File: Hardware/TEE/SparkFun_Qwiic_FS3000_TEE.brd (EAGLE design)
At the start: 25.4 x 25.4 mm, 53 parts, among them J2 QWIIC_RA, U1 FS3000

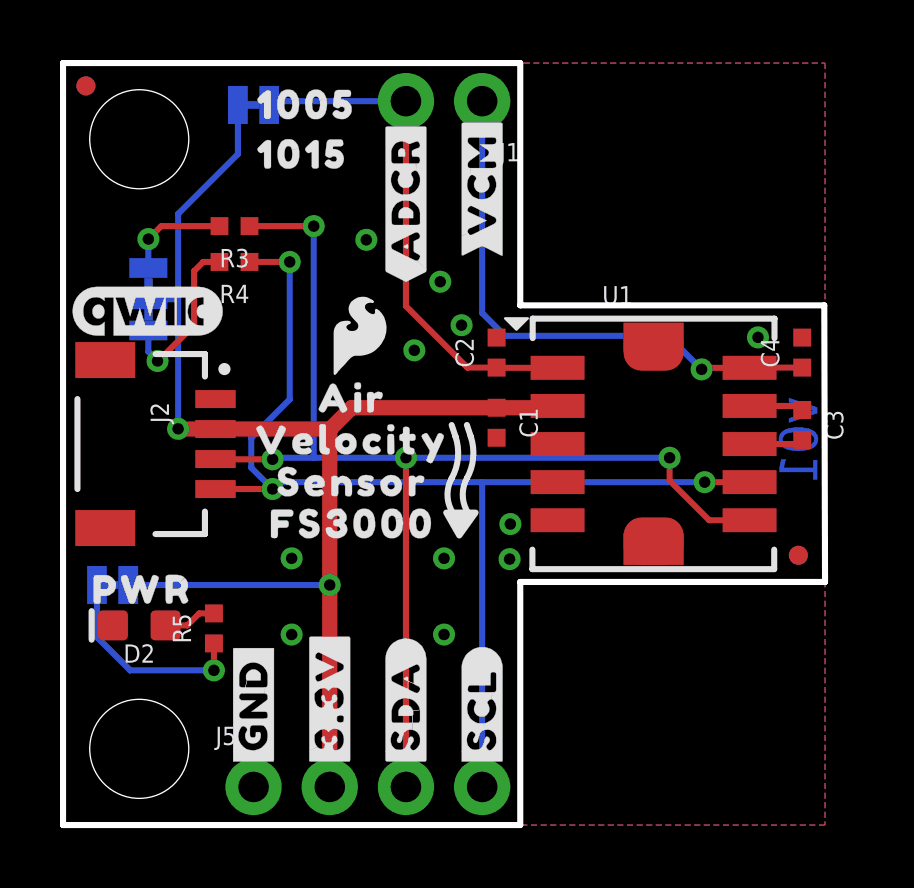
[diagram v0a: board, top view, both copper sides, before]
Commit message: eng ran checklist before double-check request
-dimensions were off grid slightly, corrected [1X1 version].
-approved DRC overlap error on jumper [1X1 version].
-added a couple more stitching GND vias [1X1]
-updated pad 3 to extend longer as shown in datasheet [both versions]
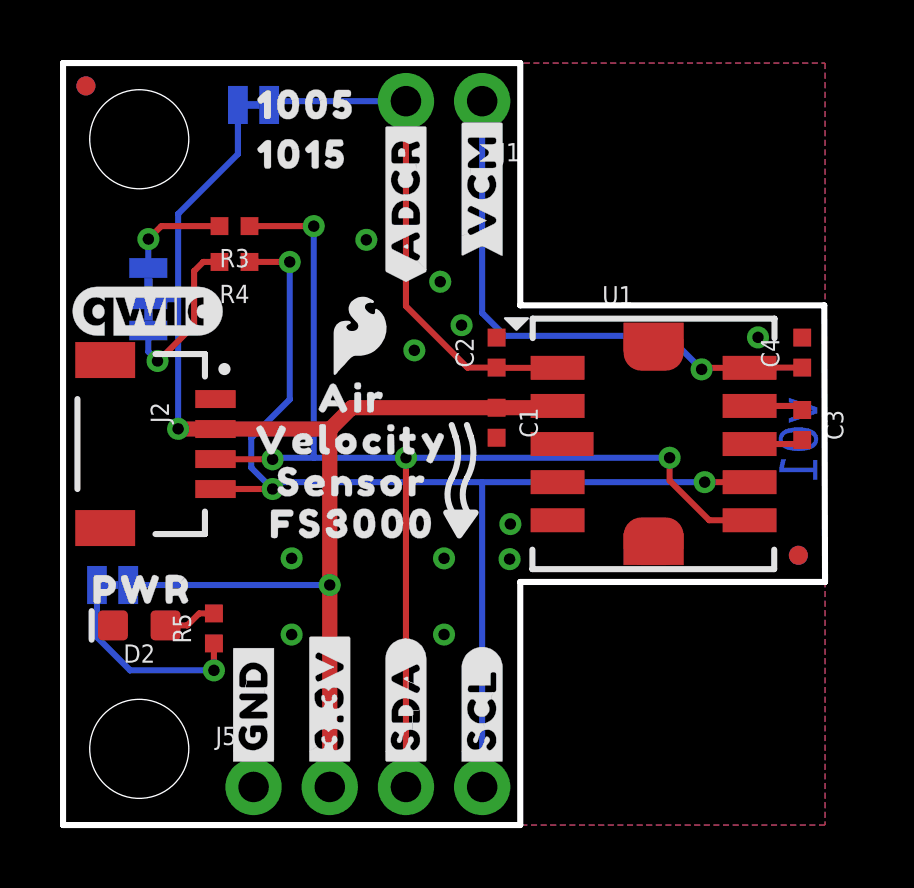
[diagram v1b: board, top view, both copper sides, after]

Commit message: updated some stuff to correct recent libraries
-GNDs, Fiducials, and standoffs were still in old library. updated.
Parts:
- JP11, JP2, JP5, JP6: device SparkFun:MICRO-FIDUCIAL -> SparkFun-Aesthetics:FIDUCIAL-MICRO
- JP3, JP8: device SparkFun:STAND-OFF -> SparkFun-Hardware:STAND-OFF
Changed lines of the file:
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@@
 <drawing>
 <settings>
-<setting alwaysvectorfont="yes"/>
+<setting alwaysvectorfont="no"/>
 <setting keepoldvectorfont="yes"/>
 <setting verticaltext="up"/>
@@
 <layer number="47" name="Measures" color="7" fill="1" visible="no" active="yes"/>
 <layer number="48" name="Document" color="7" fill="1" visible="no" active="yes"/>
-<layer number="49" name="Reference" color="7" fill="1" visible="yes" active="yes"/>
+<layer number="49" name="Reference" color="7" fill="1" visible="no" active="yes"/>
 <layer number="50" name="dxf" color="7" fill="1" visible="no" active="yes"/>
 <layer number="51" name="tDocu" color="6" fill="1" visible="yes" active="yes"/>
@@
 </autorouter>
 <elements>
-<element name="JP3" library="SparkFun" package="STAND-OFF" value="STAND-OFF" x="2.54" y="22.86" smashed="yes"/>
-<element name="JP2" library="SparkFun" package="MICRO-FIDUCIAL" value="FIDUCIALUFIDUCIAL" x="24.511" y="8.9916" smashed="yes"/>
-<element name="JP6" library="SparkFun" package="MICRO-FIDUCIAL" value="FIDUCIALUFIDUCIAL" x="0.762" y="24.638" smashed="yes"/>
+<element name="JP3" library="SparkFun-Hardware" package="STAND-OFF" value="STAND-OFF" x="2.54" y="22.86" smashed="yes"/>
+<element name="JP2" library="SparkFun-Aesthetics" package="FIDUCIAL-MICRO" value="FIDUCIALUFIDUCIAL" x="24.511" y="8.9916" smashed="yes"/>
+<element name="JP6" library="SparkFun-Aesthetics" package="FIDUCIAL-MICRO" value="FIDUCIALUFIDUCIAL" x="0.762" y="24.638" smashed="yes"/>
 <element name="R4" library="SparkFun-Resistors" package="0402-TIGHT" value="2.2k" x="5.715" y="18.7706" smashed="yes" rot="R180">
 <attribute name="NAME" x="5.715" y="18.0086" size="0.6096" layer="25" font="vector" ratio="20" rot="R180" align="bottom-center"/>
@@
 </element>
 <element name="LOGO1" library="SparkFun-Aesthetics" package="OSHW-LOGO-MINI" value="OSHW-LOGOMINI" x="23.495" y="12.954" smashed="yes" rot="MR90"/>
-<element name="JP11" library="SparkFun" package="MICRO-FIDUCIAL" value="FIDUCIALUFIDUCIAL" x="24.511" y="8.9916" smashed="yes" rot="MR0"/>
-<element name="JP5" library="SparkFun" package="MICRO-FIDUCIAL" value="FIDUCIALUFIDUCIAL" x="0.762" y="24.638" smashed="yes" rot="MR0"/>
+<element name="JP11" library="SparkFun-Aesthetics" package="FIDUCIAL-MICRO" value="FIDUCIALUFIDUCIAL" x="24.511" y="8.9916" smashed="yes" rot="MR0"/>
+<element name="JP5" library="SparkFun-Aesthetics" package="FIDUCIAL-MICRO" value="FIDUCIALUFIDUCIAL" x="0.762" y="24.638" smashed="yes" rot="MR0"/>
 <element name="J5" library="SparkFun-Connectors" package="1X04_NO_SILK" value="" x="6.35" y="1.27" smashed="yes">
 <attribute name="NAME" x="5.08" y="2.667" size="0.6096" layer="25" font="vector" ratio="20"/>
@@
 </element>
 <element name="LOGO4" library="SparkFun-Aesthetics" package="QWIIC_5MM" value="QWIIC_LOGO_5MM" x="2.794" y="17.145" smashed="yes"/>
-<element name="JP8" library="SparkFun" package="STAND-OFF" value="STAND-OFF" x="2.54" y="2.54" smashed="yes"/>
+<element name="JP8" library="SparkFun-Hardware" package="STAND-OFF" value="STAND-OFF" x="2.54" y="2.54" smashed="yes"/>
 <element name="U$5" library="output" package="#GND#0" value="" x="6.35" y="1.778" smashed="yes" rot="R90"/>
 <element name="U$6" library="output" package="#GND#0" value="" x="6.35" y="1.778" smashed="yes" rot="MR90"/>
